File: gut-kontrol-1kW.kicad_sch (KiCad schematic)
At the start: 3 parts

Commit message: Done with the powerstage
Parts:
- added C1: 220 uF, Capacitor_SMD:C_0805_2012Metric_Pad1.18x1.45mm_HandSolder, symbol Device:C_Small
- added D1: 1N4007, Diode_SMD:D_SMA-SMB_Universal_Handsoldering, symbol Device:D_Small
- added R1: 100, Resistor_SMD:R_0805_2012Metric_Pad1.20x1.40mm_HandSolder, symbol Device:R_Small
- added R3: 27, Resistor_SMD:R_0805_2012Metric_Pad1.20x1.40mm_HandSolder, symbol Device:R_Small
- added R4, R5: 10K, Resistor_SMD:R_0805_2012Metric_Pad1.20x1.40mm_HandSolder, symbol Device:R_Small
- added U1: IR2110S, Package_SO:SOIC-16W_7.5x10.3mm_P1.27mm, symbol Driver_FET:IR2110S
- R2: renamed from R?; value R_Small -> 27; footprint (none) -> Resistor_SMD:R_0805_2012Metric_Pad1.20x1.40mm_HandSolder
- gave numbers to parts that had none: 2
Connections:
- net at Q1.1 (G), R2.2: now also R4.2
- net PHASE_A: now reaches Q1.3 (S), Q2.2 (D)
- net PHASE_A: now also C1.1, R4.1, U1.6 (VS)
- net at R2.1: now also U1.8 (HO)
- net at Q2.1 (G): now also R3.2, R5.2
- net GND: now reaches Q2.3 (S)
- net GND: now also R5.1, U1.13 (SD), U1.15 (VSS), U1.2 (COM)
- net VBUS renamed +48V
- new net: C1.2, D1.1 (K), U1.7 (VB)
- new net: R3.1, U1.1 (LO)
- new net: D1.2 (A), R1.1
- new net +12V: R1.2, U1.3 (VCC)
- new net +3V3: U1.11 (VDD)
- new net HIN_A: U1.12 (HIN)
- new net LIN_A: U1.14 (LIN)
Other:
- moved on the sheet: Q1, Q2, R2

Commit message: done with powerstage board
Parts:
- added C10, C7, C8, C9: 470 uF, Capacitor_THT:CP_Radial_D16.0mm_P7.50mm, symbol Device:C_Polarized
- added C2, C3, C4: 10 uF, Capacitor_SMD:C_0805_2012Metric_Pad1.18x1.45mm_HandSolder, symbol Device:C_Small
- added C5, C6: 2.2 uF, Capacitor_SMD:C_0805_2012Metric_Pad1.18x1.45mm_HandSolder, symbol Device:C_Small
- added D2, D3: US1M, Diode_SMD:D_SMA, symbol Device:D_Small
- added J1: PHASE_A, MountingHole:MountingHole_3.2mm_M3_DIN965_Pad, symbol Connector:Screw_Terminal_01x01
- added J2: PHASE_B, MountingHole:MountingHole_3.2mm_M3_DIN965_Pad, symbol Connector:Screw_Terminal_01x01
- added J3: PHASE_C, MountingHole:MountingHole_3.2mm_M3_DIN965_Pad, symbol Connector:Screw_Terminal_01x01
- added J4: VMOT, MountingHole:MountingHole_3.2mm_M3_DIN965_Pad, symbol Connector:Screw_Terminal_01x01
- added J5: GND, MountingHole:MountingHole_3.2mm_M3_DIN965_Pad, symbol Connector:Screw_Terminal_01x01
- added J6: STEPDOWN, Connector_PinHeader_2.54mm:PinHeader_1x02_P2.54mm_Vertical, symbol Connector_Generic:Conn_01x02
- added J7: Conn_01x12, symbol Connector_Generic:Conn_01x12
- added Q3, Q4, Q5, Q6: IRFb4110N, Package_TO_SOT_THT:TO-220-3_Vertical, symbol Transistor_FET:IRF540N
- added R10, R11, R8, R9: 27, Resistor_SMD:R_0805_2012Metric_Pad1.20x1.40mm_HandSolder, symbol Device:R_Small
- added R12, R13, R14, R15: 10K, Resistor_SMD:R_0805_2012Metric_Pad1.20x1.40mm_HandSolder, symbol Device:R_Small
- added R6, R7: 100, Resistor_SMD:R_0805_2012Metric_Pad1.20x1.40mm_HandSolder, symbol Device:R_Small
- added U2, U5, U6: ACS756xCB-050B-PFF, Sensor_Current:Allegro_CB_PFF, symbol Sensor_Current:ACS756xCB-050B-PFF
- added U3, U4: IR2110S, Package_SO:SOIC-16W_7.5x10.3mm_P1.27mm, symbol Driver_FET:IR2110S
- C1: value 220 uF -> 2.2 uF
- D1: value 1N4007 -> US1M; footprint Diode_SMD:D_SMA-SMB_Universal_Handsoldering -> Diode_SMD:D_SMA
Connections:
- net +12V: now also J6.1 (Pin_1), J7.1 (Pin_1), J7.2 (Pin_2), R6.2, R7.2, U3.3 (VCC), U4.3 (VCC)
- net +3V3: now also C2.2, C3.2, C4.2, J7.10 (Pin_10), J7.9 (Pin_9), U2.1 (VCC), U3.11 (VDD), U4.11 (VDD), U5.1 (VCC), U6.1 (VCC)
- net +48V: now also C10.1, C7.1, C8.1, C9.1, J4.1 (Pin_1), Q3.2 (D), Q5.2 (D)
- net GND: now also C10.2, C2.1, C3.1, C4.1, C7.2, C8.2, C9.2, J5.1 (Pin_1), J6.2 (Pin_2), J7.11 (Pin_11), J7.12 (Pin_12), Q4.3 (S), Q6.3 (S), R13.1, R15.1, U2.2 (GND), U3.13 (SD), U3.15 (VSS), U3.2 (COM), U4.13 (SD), U4.15 (VSS), U4.2 (COM), U5.2 (GND), U6.2 (GND)
- net HIN_A: now also J7.3 (Pin_3)
- net LIN_A: now also J7.4 (Pin_4)
- net PHASE_A: now also U2.4 (IP+)
- new net: C5.2, D2.1 (K), U3.7 (VB)
- new net: D2.2 (A), R6.1
- new net: D3.2 (A), R7.1
- new net: Q5.1 (G), R10.2, R14.2
- new net: R11.1, U4.1 (LO)
- new net: C6.2, D3.1 (K), U4.7 (VB)
- new net: R10.1, U4.8 (HO)
- new net: Q6.1 (G), R11.2, R15.2
- new net: Q4.1 (G), R13.2, R9.2
- new net: R8.1, U3.8 (HO)
- new net: Q3.1 (G), R12.2, R8.2
- new net: R9.1, U3.1 (LO)
- new net A_CURRENT_SENS: U2.3 (VIOUT)
- new net B_CURRENT_SENS: U5.3 (VIOUT)
- new net C_CURRENT_SENS: U6.3 (VIOUT)
- new net HIN_B: J7.5 (Pin_5), U3.12 (HIN)
- new net HIN_C: J7.7 (Pin_7), U4.12 (HIN)
- new net LIN_B: J7.6 (Pin_6), U3.14 (LIN)
- new net LIN_C: J7.8 (Pin_8), U4.14 (LIN)
- new net PHASE_A_OUT: J1.1 (Pin_1), U2.5 (IP-)
- new net PHASE_B: C5.1, Q3.3 (S), Q4.2 (D), R12.1, U3.6 (VS), U5.4 (IP+)
- new net PHASE_B_OUT: J2.1 (Pin_1), U5.5 (IP-)
- new net PHASE_C: C6.1, Q5.3 (S), Q6.2 (D), R14.1, U4.6 (VS), U6.4 (IP+)
- new net PHASE_C_OUT: J3.1 (Pin_1), U6.5 (IP-)
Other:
- note added: "TODO: Cari dioda 1A"
- note added: "TODO: Cek epsilon, copper weight di PCBway"
- moved on the sheet: C1, D1, Q1, Q2, R1, R2, R3, R4, R5, U1

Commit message: Adding connector and CAD viz
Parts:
- removed J6: STEPDOWN, Connector_PinHeader_2.54mm:PinHeader_1x02_P2.54mm_Vertical, symbol Connector_Generic:Conn_01x02
- added C11, C12, C13, C14, C15, C16: 0.1 uF, Capacitor_SMD:C_0805_2012Metric_Pad1.18x1.45mm_HandSolder, symbol Device:C_Small
- added J10: PHASE_C_ISENSE, Connector_PinSocket_2.54mm:PinSocket_1x03_P2.54mm_Vertical, symbol Connector_Generic:Conn_01x03
- added J8: PHASE_A_ISENSE, Connector_PinSocket_2.54mm:PinSocket_1x03_P2.54mm_Vertical, symbol Connector_Generic:Conn_01x03
- added J9: PHASE_B_ISENSE, Connector_PinSocket_2.54mm:PinSocket_1x03_P2.54mm_Vertical, symbol Connector_Generic:Conn_01x03
- added R16, R17, R18: 100, Resistor_SMD:R_0805_2012Metric_Pad1.20x1.40mm_HandSolder, symbol Device:R_Small
- C1: footprint Capacitor_SMD:C_0805_2012Metric_Pad1.18x1.45mm_HandSolder -> Connector_PinHeader_2.54mm:PinHeader_1x03_P2.54mm_Vertical
- J7: footprint (none) -> Connector_PinHeader_2.54mm:PinHeader_2x12_P2.54mm_Vertical
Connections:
- net +3V3: now also C14.2, C15.2, C16.2, J10.1 (Pin_1), J8.1 (Pin_1), J9.1 (Pin_1)
- net GND: now also C11.1, C12.1, C13.1, C14.1, C15.1, C16.1, J10.3 (Pin_3), J8.3 (Pin_3), J9.3 (Pin_3)
- net A_CURRENT_SENS: no longer names the net of U2.3 (VIOUT)
- net A_CURRENT_SENS: now also R16.1
- net B_CURRENT_SENS: no longer names the net of U5.3 (VIOUT)
- net B_CURRENT_SENS: now also R17.1
- net C_CURRENT_SENS: no longer names the net of U6.3 (VIOUT)
- net C_CURRENT_SENS: now also R18.1
- new net: C13.2, J10.2 (Pin_2), R18.2
- new net: C12.2, J9.2 (Pin_2), R17.2
- new net: C11.2, J8.2 (Pin_2), R16.2

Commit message: major fix in conn footprint, bootsrap error, etc
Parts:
- added U7: XT30PW-F, XT30PW-F:XT30PW-F, symbol XT30PW-F:XT30PW-F
- C1: footprint Connector_PinHeader_2.54mm:PinHeader_1x03_P2.54mm_Vertical -> Capacitor_SMD:C_0805_2012Metric_Pad1.18x1.45mm_HandSolder
- J7: footprint Connector_PinHeader_2.54mm:PinHeader_2x12_P2.54mm_Vertical -> Connector_PinHeader_2.54mm:PinHeader_1x12_P2.54mm_Vertical
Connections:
- net +12V: now also U7.P2 (+); no longer J7.1 (Pin_1), J7.2 (Pin_2)
- net +3V3: now also J7.1 (Pin_1), J7.2 (Pin_2)
- net GND: now also U7.P1 (-)

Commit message: Nambah Skematik
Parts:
- added CFF1, CFF2: 33nF, symbol Device:C
- added CIN1, CIN2: 33uF/100W, symbol Device:C_Polarized_US
- added COUT1, COUT2: 100uF/35V, symbol Device:C_Polarized_US
- added D4, D5: S310, symbol Device:D_Zener
- added L1, L2: 100uH/1A, symbol Device:L
- added R19: 26K, symbol Device:R
- added R20: 3K, symbol Device:R
- added R21: 6.5K, symbol Device:R
- added R22: 20K, symbol Device:R
- added XL1, XL2: ~, symbol Custom_Library:XL7015
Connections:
- net +12V: now also CFF1.1, COUT1.1, L1.2, R19.1
- net +48V: now also CIN1.1, CIN2.1, XL1.1 (V_IN), XL2.1 (V_IN)
- net GND: now also CIN1.2, CIN2.2, COUT1.2, COUT2.2, D4.2 (A), D5.2 (A), R20.2, R21.2, XL1.3 (GND), XL2.3 (GND)
- new net: CFF1.2, R19.2, R20.1, XL1.4 (FB)
- new net: D4.1 (K), L1.1, XL1.2 (SW)
- new net: D5.1 (K), L2.1, XL2.2 (SW)
- new net: CFF2.2, R21.1, R22.2, XL2.4 (FB)
- new net +5V: CFF2.1, COUT2.1, L2.2, R22.1
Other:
- moved on the sheet: C1, C11, C12, C13, C14, C15, C16, C2, C3, C4, C5, C6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

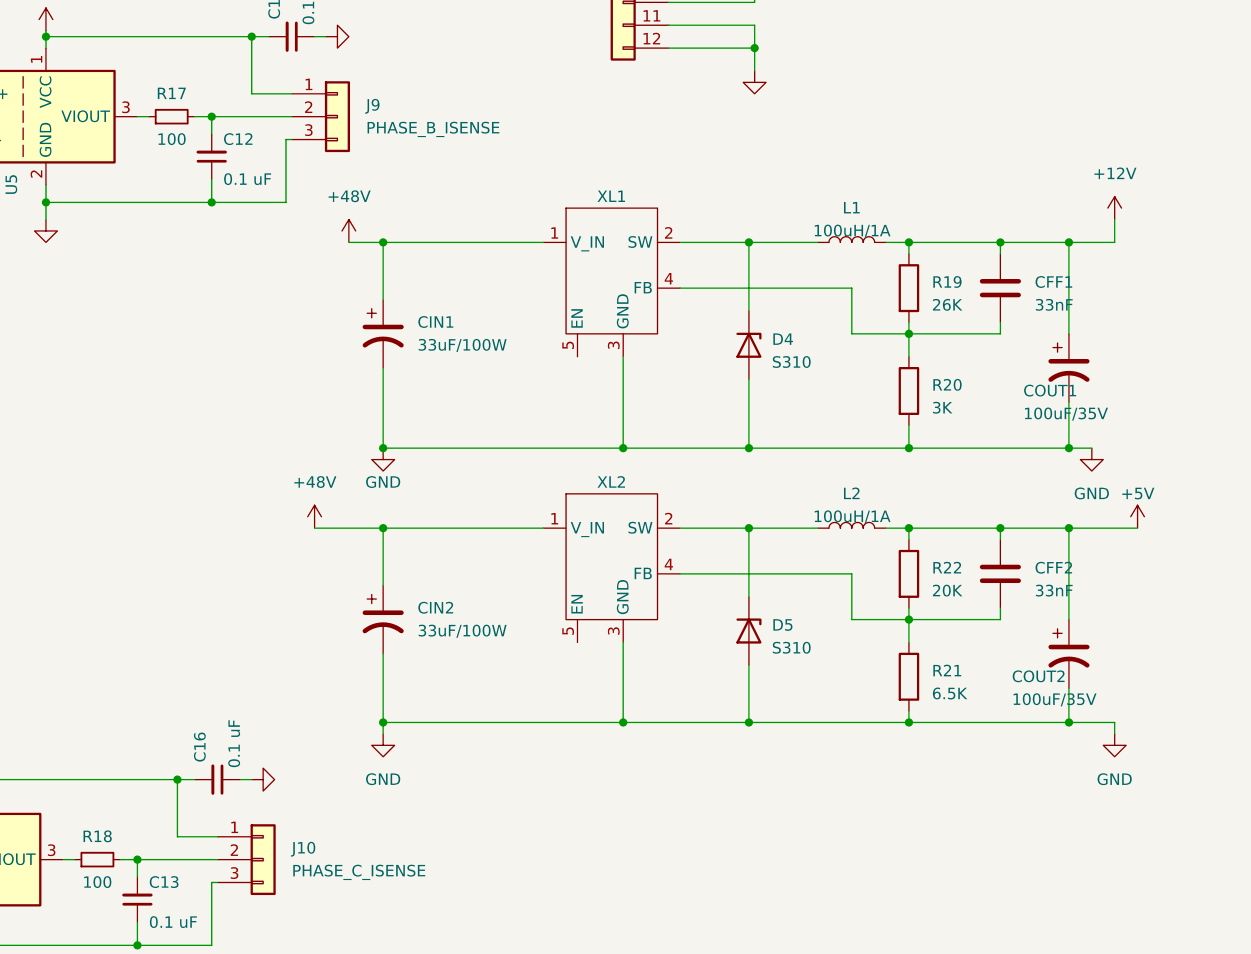
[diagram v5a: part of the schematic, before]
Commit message: ganti heatsink
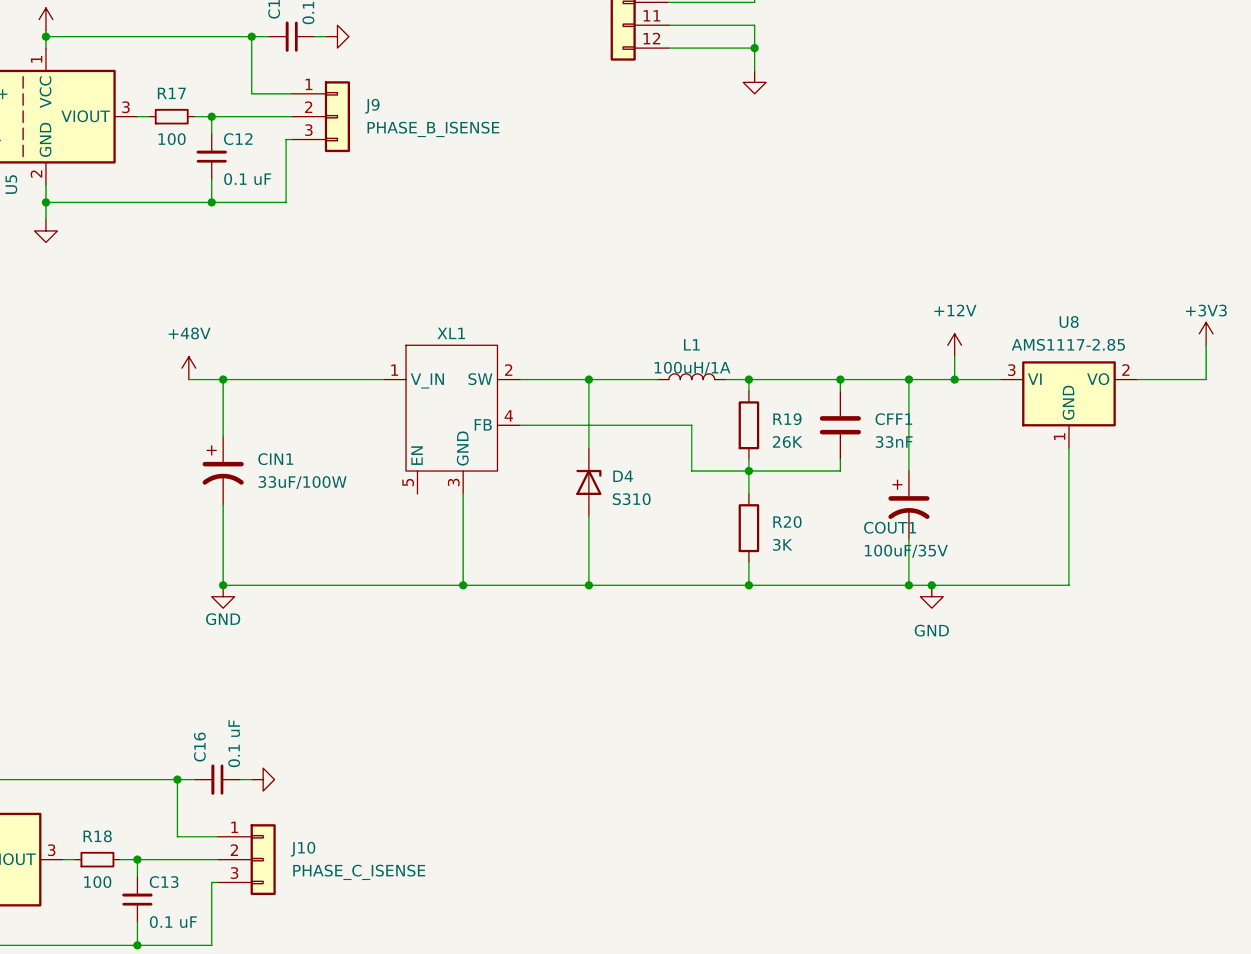
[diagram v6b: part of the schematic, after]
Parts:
- removed CFF2: 33nF, symbol Device:C
- removed CIN2: 33uF/100W, symbol Device:C_Polarized_US
- removed COUT2: 100uF/35V, symbol Device:C_Polarized_US
- removed D5: S310, symbol Device:D_Zener
- removed L2: 100uH/1A, symbol Device:L
- removed R21: 6.5K, symbol Device:R
- removed R22: 20K, symbol Device:R
- removed XL2: ~, symbol Custom_Library:XL7015
- added U8: AMS1117-2.85, Package_TO_SOT_SMD:SOT-223-3_TabPin2, symbol Regulator_Linear:AMS1117-2.85
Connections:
- net +12V: now also U8.3 (VI)
- net +3V3: now also U8.2 (VO)
- net GND: now also U8.1 (GND)
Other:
- moved on the sheet: CFF1, CIN1, COUT1, D4, L1, R19, R20, XL1

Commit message: Layout PCB
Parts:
- CFF1, R19, R20: footprint (none) -> Resistor_SMD:R_0805_2012Metric
- CIN1, COUT1: footprint (none) -> Capacitor_THT:CP_Radial_D8.0mm_P3.50mm
- D4: footprint (none) -> Diode_SMD:D_SMA
- J7: footprint Connector_PinHeader_2.54mm:PinHeader_1x12_P2.54mm_Vertical -> Connector_PinHeader_2.54mm:PinHeader_2x06_P2.54mm_Vertical
- L1: footprint (none) -> Inductor_SMD:L_10.4x10.4_H4.8
- XL1: footprint (none) -> Package_TO_SOT_SMD:TO-252-5_TabPin3
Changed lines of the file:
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@@
       (effects (font (size 1.27 1.27)) (justify left))
     )
-    (property "Footprint" "" (at 219.202 120.65 90)
+    (property "Footprint" "Resistor_SMD:R_0805_2012Metric" (at 219.202 120.65 90)
       (effects (font (size 1.27 1.27)) hide)
     )
@@
       (effects (font (size 1.27 1.27)) (justify left))
     )
-    (property "Footprint" "" (at 203.2 127 0)
+    (property "Footprint" "Diode_SMD:D_SMA" (at 203.2 127 0)
       (effects (font (size 1.27 1.27)) hide)
     )
@@
       (effects (font (size 1.27 1.27)))
     )
-    (property "Footprint" "" (at 191.77 128.27 0)
+    (property "Footprint" "Package_TO_SOT_SMD:TO-252-5_TabPin3" (at 191.77 128.27 0)
       (effects (font (size 1.27 1.27)) hide)
     )
@@
       (effects (font (size 1.27 1.27)) (justify left))
     )
-    (property "Footprint" "" (at 238.76 129.54 0)
+    (property "Footprint" "Capacitor_THT:CP_Radial_D8.0mm_P3.50mm" (at 238.76 129.54 0)
       (effects (font (size 1.27 1.27)) hide)
     )
@@
       (effects (font (size 1.27 1.27)) (justify left))
     )
-    (property "Footprint" "" (at 219.202 132.08 90)
+    (property "Footprint" "Resistor_SMD:R_0805_2012Metric" (at 219.202 132.08 90)
       (effects (font (size 1.27 1.27)) hide)
     )
@@
       (effects (font (size 1.27 1.27)) (justify left))
     )
-    (property "Footprint" "" (at 232.1052 124.46 0)
+    (property "Footprint" "Resistor_SMD:R_0805_2012Metric" (at 232.1052 124.46 0)
       (effects (font (size 1.27 1.27)) hide)
     )
@@
       (effects (font (size 1.27 1.27)))
     )
-    (property "Footprint" "Connector_PinHeader_2.54mm:PinHeader_1x12_P2.54mm_Vertical" (at 207.01 63.5 0)
+    (property "Footprint" "Connector_PinHeader_2.54mm:PinHeader_2x06_P2.54mm_Vertical" (at 207.01 63.5 0)
       (effects (font (size 1.27 1.27)) hide)
     )
@@
       (effects (font (size 1.27 1.27)) (justify left))
     )
-    (property "Footprint" "" (at 162.56 125.73 0)
+    (property "Footprint" "Capacitor_THT:CP_Radial_D8.0mm_P3.50mm" (at 162.56 125.73 0)
       (effects (font (size 1.27 1.27)) hide)
     )
@@
       (effects (font (size 1.27 1.27)))
     )
-    (property "Footprint" "" (at 214.63 115.57 0)
-      (effects (font (size 1.27 1.27)) hide)
-    )
+    (property "Footprint" "Inductor_SMD:L_10.4x10.4_H4.8" (at 214.63 115.57 0)
+      (effects (font (size 1.27 1.27)) hide)
+    )

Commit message: nambah rev number
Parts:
- removed U7: XT30PW-F, XT30PW-F:XT30PW-F, symbol XT30PW-F:XT30PW-F
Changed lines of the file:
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@@
-    (stroke (width 0) (type default))
-  )
-  (wire (pts (xy 236.855 52.07) (xy 240.03 52.07))
     (stroke (width 0) (type default))
   )
@@
     (stroke (width 0) (type default))
   )
-  (wire (pts (xy 236.855 54.61) (xy 240.03 54.61))
-    (stroke (width 0) (type default))
-  )
   (wire (pts (xy 198.12 38.1) (xy 198.12 42.545))
     (stroke (width 0) (type default))
@@
     (stroke (width 0) (type default))
   )
-  (wire (pts (xy 236.855 49.53) (xy 236.855 52.07))
-    (stroke (width 0) (type default))
-  )
   (wire (pts (xy 165.735 160.02) (xy 164.465 160.02))
     (stroke (width 0) (type default))
@@
   )
   (wire (pts (xy 151.13 168.91) (xy 153.035 168.91))
-    (stroke (width 0) (type default))
-  )
-  (wire (pts (xy 236.855 59.055) (xy 236.855 54.61))
     (stroke (width 0) (type default))
   )
@@
     )
   )
-  (symbol (lib_id "power:GND") (at 236.855 59.055 0) (unit 1)
-    (in_bom yes) (on_board yes) (dnp no) (fields_autoplaced)
-    (property "Reference" "#PWR03" (at 236.855 65.405 0)
-      (effects (font (size 1.27 1.27)) hide)
-    )
-    (property "Value" "GND" (at 236.855 64.135 0)
-      (effects (font (size 1.27 1.27)) hide)
-    )
-    (property "Footprint" "" (at 236.855 59.055 0)
-      (effects (font (size 1.27 1.27)) hide)
-    )
-    (property "Datasheet" "" (at 236.855 59.055 0)
-      (effects (font (size 1.27 1.27)) hide)
-    )
-    (pin "1")
-    (instances
-      (project "gut-kontrol-1kW"
-        (path "/641c74a3-ac72-4365-a2c2-8bde74996601"
-          (reference "#PWR03") (unit 1)
-        )
-      )
-    )
-  )
   (symbol (lib_id "power:+12V") (at 42.545 147.32 0) (unit 1)
     (in_bom yes) (on_board yes) (dnp no)
@@
         )
       )
-    )
-  )
-  (symbol (lib_id "power:+12V") (at 236.855 49.53 0) (unit 1)
-    (in_bom yes) (on_board yes) (dnp no)
-    (property "Reference" "#PWR02" (at 236.855 53.34 0)
-      (effects (font (size 1.27 1.27)) hide)
-    )
-    (property "Value" "+12V" (at 236.855 44.45 0)
-      (effects (font (size 1.27 1.27)))
-    )
-    (property "Footprint" "" (at 236.855 49.53 0)
-      (effects (font (size 1.27 1.27)) hide)
-    )
-    (property "Datasheet" "" (at 236.855 49.53 0)
-      (effects (font (size 1.27 1.27)) hide)
-    )
-    (pin "1")
-    (instances
-      (project "gut-kontrol-1kW"
-        (path "/641c74a3-ac72-4365-a2c2-8bde74996601"
-          (reference "#PWR02") (unit 1)
-        )
-      )
-    )
-  )
-  (symbol (lib_id "XT30PW-F:XT30PW-F") (at 247.65 54.61 0) (mirror y) (unit 1)
-    (in_bom yes) (on_board yes) (dnp no) (fields_autoplaced)
-    (property "Reference" "U7" (at 251.46 52.705 0)
-      (effects (font (size 1.27 1.27)) (justify right))
-    )
-    (property "Value" "XT30PW-F" (at 251.46 55.245 0)
-      (effects (font (size 1.27 1.27)) (justify right))
-    )
-    (property "Footprint" "XT30PW-F:XT30PW-F" (at 247.65 54.61 0)
-      (effects (font (size 1.27 1.27)) (justify bottom) hide)
-    )
-    (property "Datasheet" "" (at 247.65 54.61 0)
-      (effects (font (size 1.27 1.27)) hide)
-    )
-    (pin "P1")
-    (pin "P2")
-    (instances
-      (project "gut-kontrol-1kW"
-        (path "/641c74a3-ac72-4365-a2c2-8bde74996601"
-          (reference "U7") (unit 1)
-        )
-      )
